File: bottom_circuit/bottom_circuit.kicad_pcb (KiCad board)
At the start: 2 copper layers, 37.7 x 37.7 mm, 0 parts

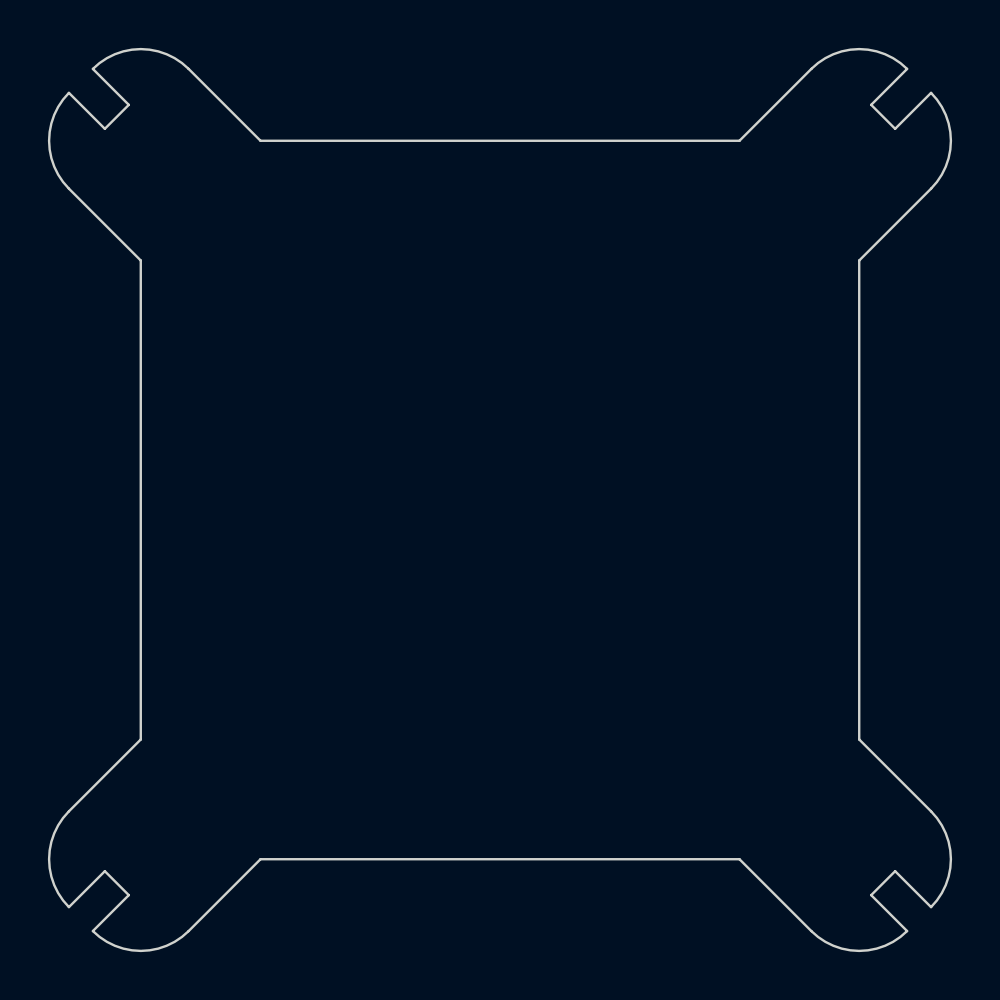
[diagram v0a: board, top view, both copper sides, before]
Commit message: bottom PCB and updated GPS/TOF port on top PCB set up
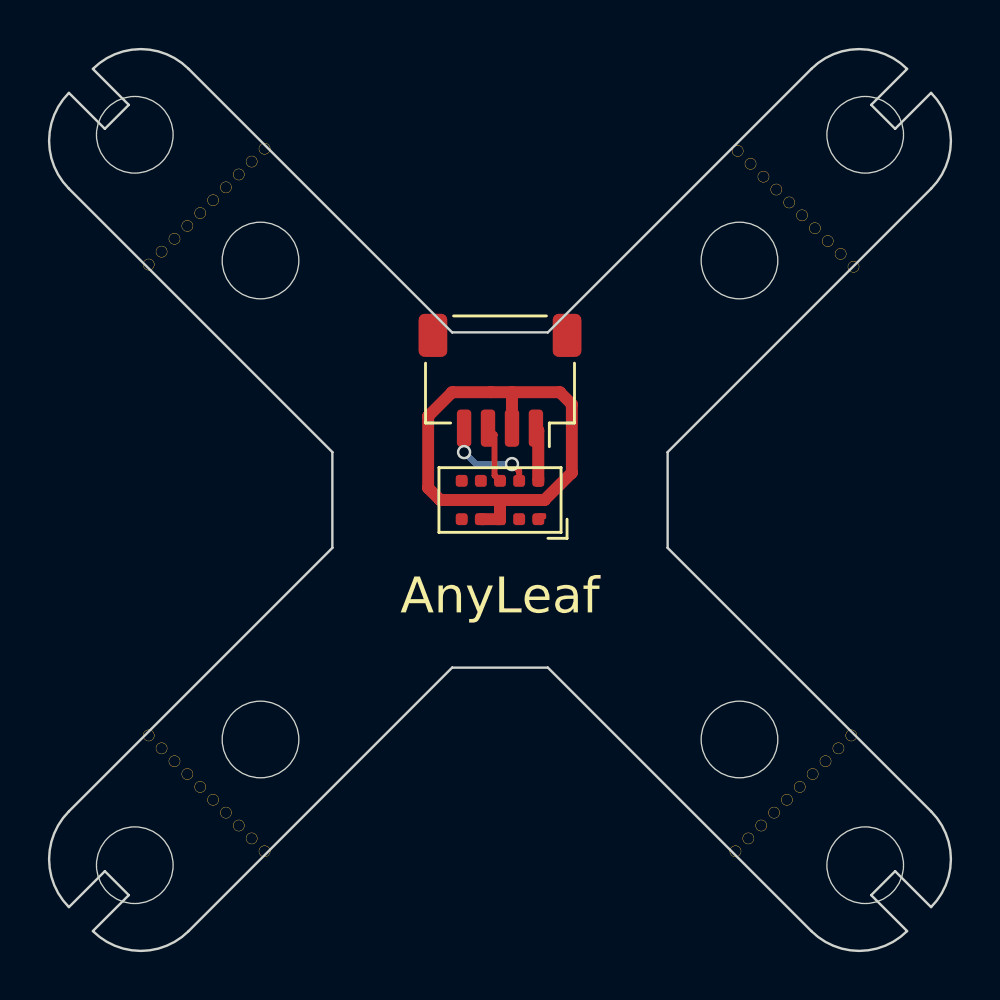
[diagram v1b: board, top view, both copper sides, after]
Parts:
- added H1: MountingHole, MountingHole:MountingHole_3.2mm_M3, F.Cu at (134.8, 84.8)
- added H10: MountingHole, MountingHole:MountingHole_3.2mm_M3, F.Cu at (160.0, 110.0)
- added H11: MountingHole_Pad, Anyleaf_Shared:Mouse bites_7mm, F.Cu at (137.8, 112.2)
- added H12: MountingHole_Pad, Anyleaf_Shared:Mouse bites_7mm, F.Cu at (137.8, 87.8)
- added H2: MountingHole, MountingHole:MountingHole_3.2mm_M3, F.Cu at (165.2, 84.8)
- added H3: MountingHole, MountingHole:MountingHole_3.2mm_M3, F.Cu at (134.8, 115.2)
- added H4: MountingHole, MountingHole:MountingHole_3.2mm_M3, F.Cu at (165.2, 115.2)
- added H5: MountingHole_Pad, Anyleaf_Shared:Mouse bites_7mm, F.Cu at (162.3, 87.8)
- added H6: MountingHole_Pad, Anyleaf_Shared:Mouse bites_7mm, F.Cu at (162.2, 112.2)
- added H7: MountingHole, MountingHole:MountingHole_3.2mm_M3, F.Cu at (140.0, 90.0)
- added H8: MountingHole, MountingHole:MountingHole_3.2mm_M3, F.Cu at (160.0, 90.0)
- added H9: MountingHole, MountingHole:MountingHole_3.2mm_M3, F.Cu at (140.0, 110.0)
- added J1: Conn_01x04_Male, Connector_JST:JST_SH_SM04B-SRSS-TB_1x04-1MP_P1.00mm_Horizontal, F.Cu at (150.0, 95.0)
- added U1: VL53L1CXV0FY1, Sensor_Distance:ST_VL53L1x, F.Cu at (150.0, 100.0)
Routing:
- net GND: track 0.00 -> 22.9 mm
- net /SCL: track 0.00 -> 4.03 mm, vias 0 -> 2
- net /SDA: track 0.00 -> 2.41 mm
- net +3V3: track 0.00 -> 2.24 mm
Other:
- outline, holes or cut-outs redrawn
- board text added: "AnyLeaf"

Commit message: added tx pwr enum, and pass to preflight
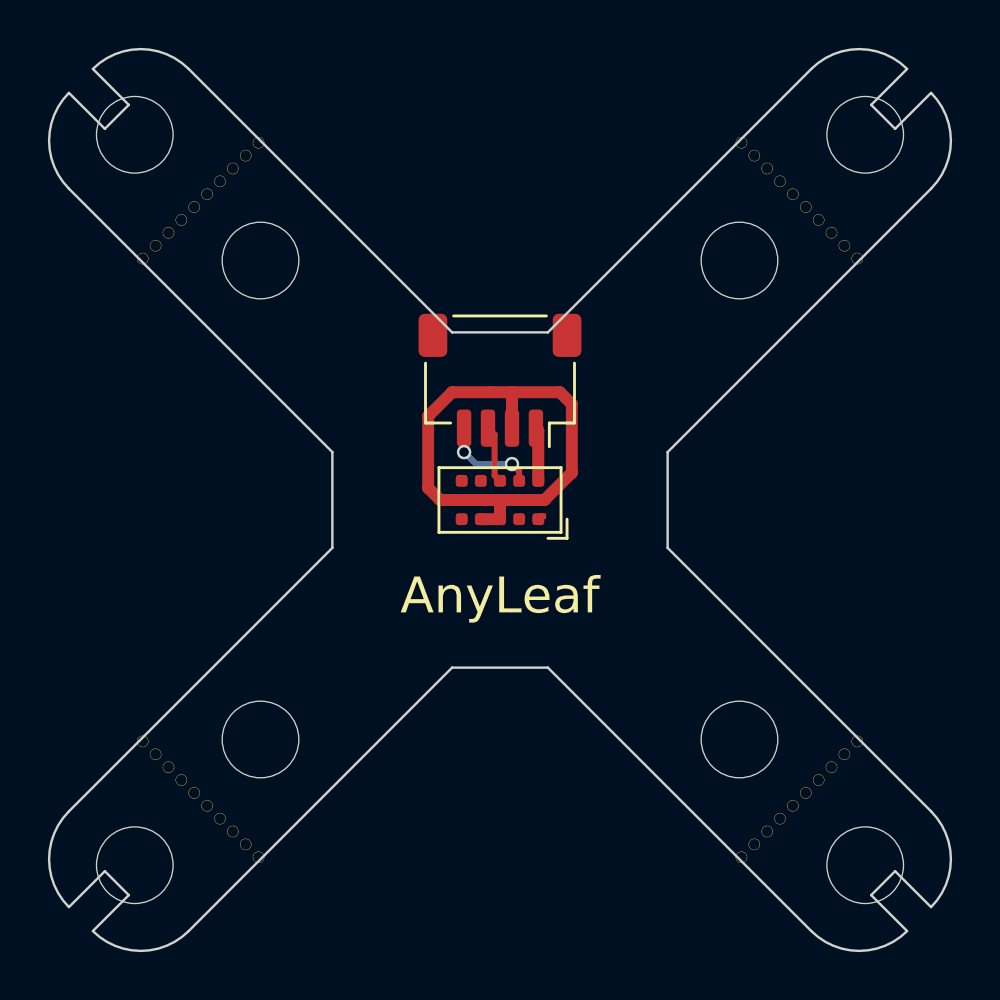
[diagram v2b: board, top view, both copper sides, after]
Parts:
- moved H5 0.38 mm to (162.5, 87.5)
- moved H11 0.35 mm to (137.5, 112.5)
- moved H12 0.35 mm to (137.5, 87.5)
- moved H6 0.35 mm to (162.5, 112.5)
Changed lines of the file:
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@@
   (net 9 "/SCL")
   (footprint "Anyleaf_Shared:Mouse bites_7mm" (layer "F.Cu")
-    (at 137.75 87.75 45)
+    (at 137.5 87.5 45)
     (property "Sheetfile" "bottom_circuit.kicad_sch")
     (property "Sheetname" "")
@@
   )
   (footprint "Anyleaf_Shared:Mouse bites_7mm" (layer "F.Cu")
-    (at 137.75 112.25 135)
+    (at 137.5 112.5 135)
     (property "Sheetfile" "bottom_circuit.kicad_sch")
     (property "Sheetname" "")
@@
   )
   (footprint "Anyleaf_Shared:Mouse bites_7mm" (layer "F.Cu")
-    (at 162.25 112.25 45)
+    (at 162.5 112.5 45)
     (property "Sheetfile" "bottom_circuit.kicad_sch")
     (property "Sheetname" "")
@@
   )
   (footprint "Anyleaf_Shared:Mouse bites_7mm" (layer "F.Cu")
-    (at 162.343503 87.843503 135)
-    (property "Sheetfile" "bottom_circuit.kicad_sch")
-    (property "Sheetname" "")
+    (at 162.5 87.5 135)
+    (property "Sheetfile" "bottom_circuit.kicad_sch")
+    (property "Sheetname" "")
